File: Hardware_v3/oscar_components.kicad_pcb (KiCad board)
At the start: 4 copper layers, 71 x 100 mm, 71 parts, among them J1 SWD_Header, J10 MIDI_THROUGH, J11 USB_C_Receptacle, J12 Debug_Header, J2 Eurorack_10_pin_power, J3 ChannelC_In, J4 ChannelA_In, J5 ChannelB_In, J6 ChC_Buff_Out, J7 ChA_Buff_Out, J8 ChB_Buff_Out, J9 MIDI_IN, SW1 Reset_Button, SW2 Menu_Button, SW3 Left_Encoder, SW4 Right_Encoder, U1 LT1117-3.3, U2 ILI9341_SPI_Daughterboard, U3 STM32F446RETx, U4 TL074, U5 MCP6004, U6 H11L1, Y1 8MHz

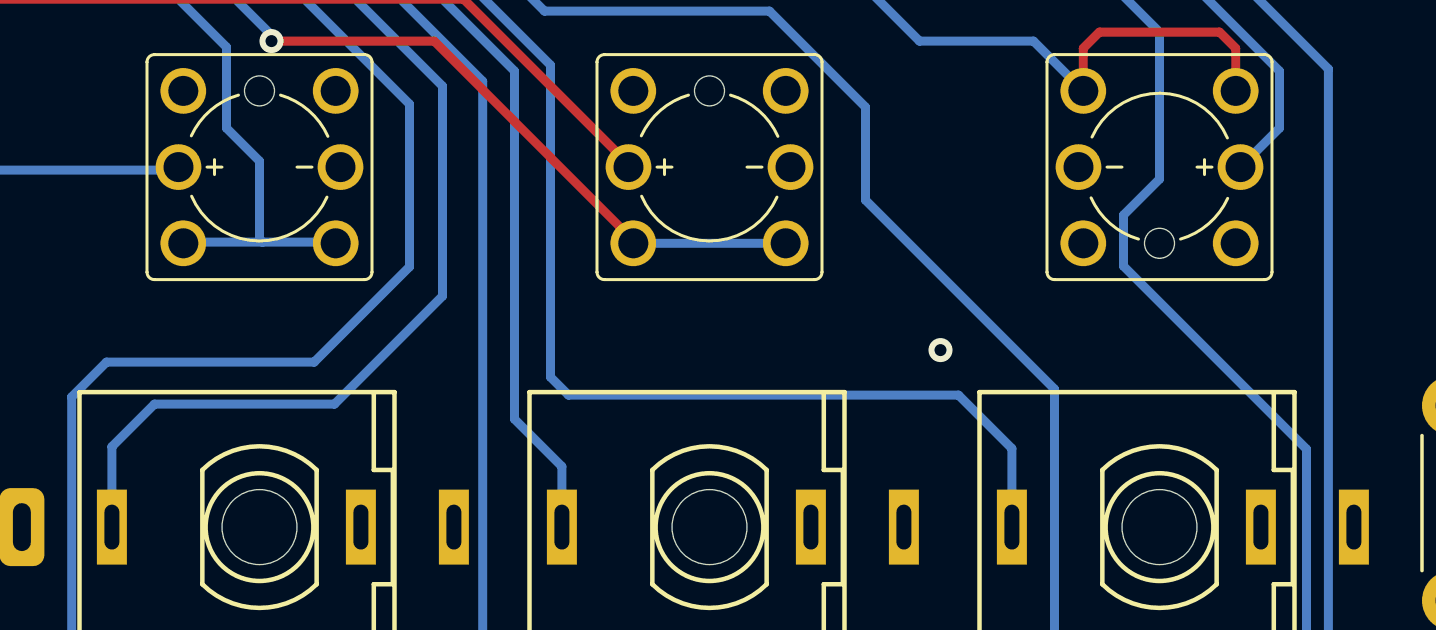
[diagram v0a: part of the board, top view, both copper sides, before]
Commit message: Work on Build Guide; Clean up old folders
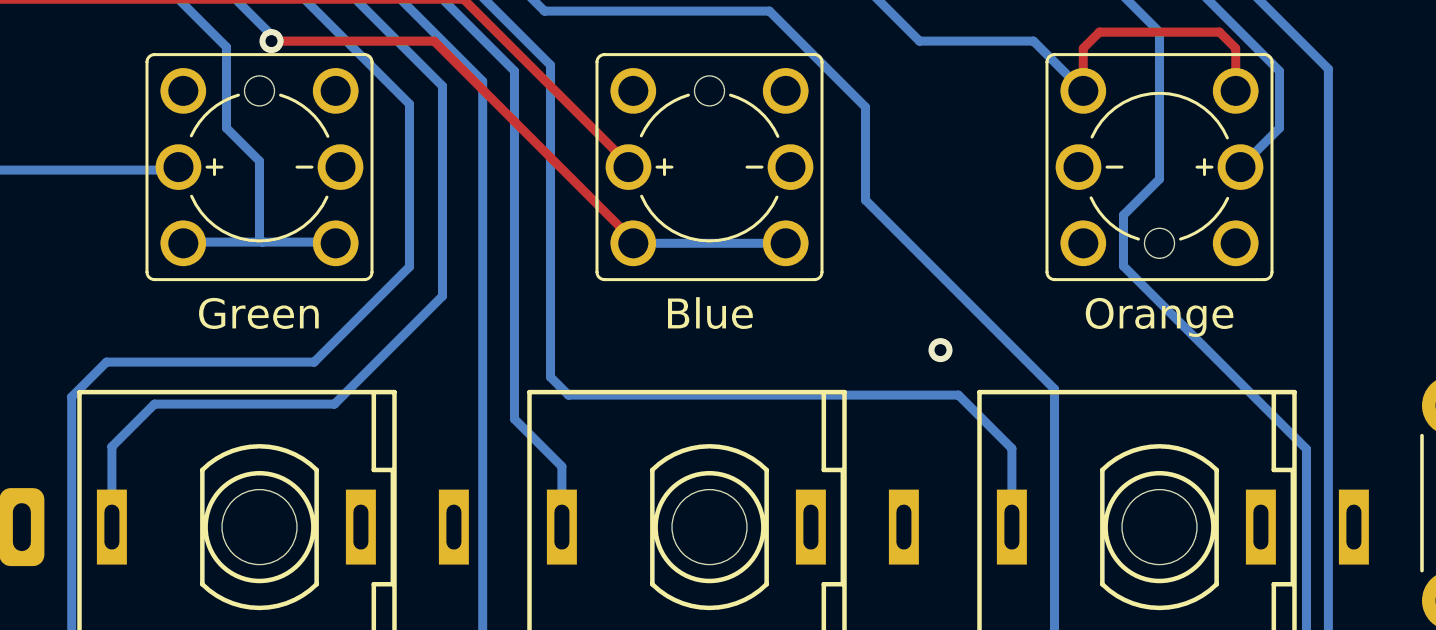
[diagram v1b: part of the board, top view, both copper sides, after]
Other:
- board text added: "Blue"
- board text added: "Green"
- board text added: "Orange"
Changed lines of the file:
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@@
 		(sheetname "Root")
 		(sheetfile "oscar_components.kicad_sch")
-		(attr through_hole)
+		(attr through_hole exclude_from_pos_files exclude_from_bom)
 		(fp_line
 			(start -1.27 1.27)
@@
 		(sheetname "Root")
 		(sheetfile "oscar_components.kicad_sch")
-		(attr through_hole)
+		(attr through_hole exclude_from_pos_files exclude_from_bom)
 		(fp_line
 			(start -5.07 -3.2)
@@
 		(sheetname "Root")
 		(sheetfile "oscar_components.kicad_sch")
-		(attr through_hole)
+		(attr through_hole exclude_from_pos_files exclude_from_bom)
 		(fp_line
 			(start -1.33 -6.41)
@@
 		)
 	)
+	(gr_text "Green"
+		(at 122 125.5 0)
+		(layer "F.SilkS")
+		(effects
+			(font
+				(size 1 1)
+				(thickness 0.15)
+			)
+			(justify bottom)
+		)
+	)
+	(gr_text "Blue"
+		(at 137 125.5 0)
+		(layer "F.SilkS")
+		(effects
+			(font
+				(size 1 1)
+				(thickness 0.15)
+			)
+			(justify bottom)
+		)
+	)
+	(gr_text "Orange"
+		(at 152 125.5 0)
+		(layer "F.SilkS")
+		(effects
+			(font
+				(size 1 1)
+				(thickness 0.15)
+			)
+			(justify bottom)
+		)
+	)

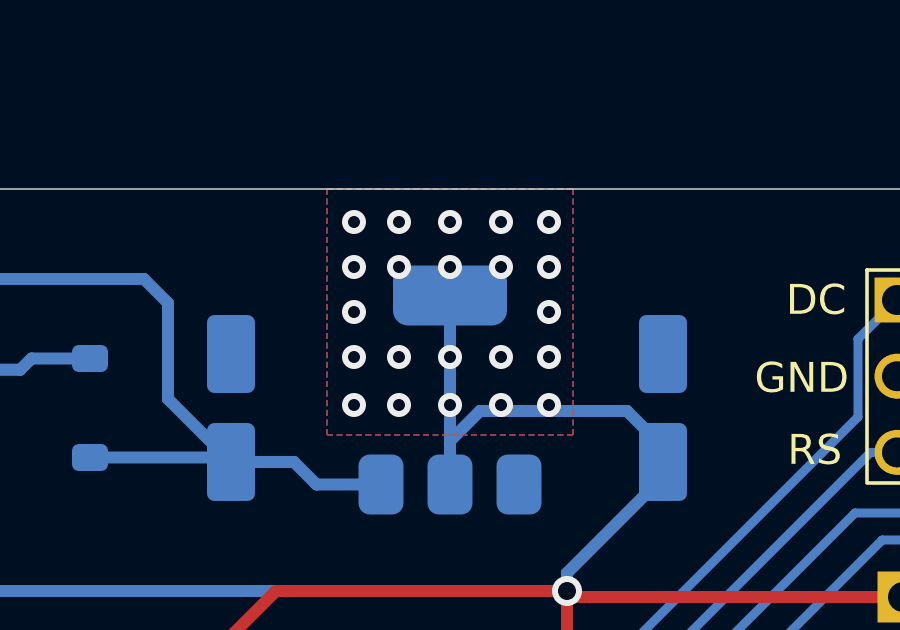
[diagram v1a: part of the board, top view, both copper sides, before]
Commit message: Increased size of regulator heat sink vias
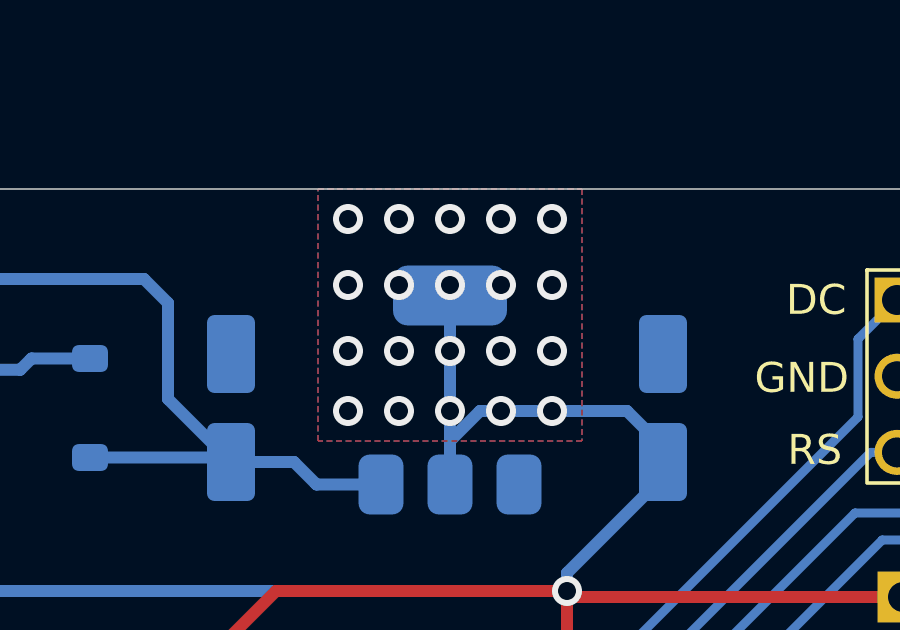
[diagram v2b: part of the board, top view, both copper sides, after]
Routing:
- net +3.3V: vias 28 -> 26
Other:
- board text added: "Oscar v3.1 Mountjoy Modular 2025"
- board text removed: "Oscar v3 Mountjoy Modular 2025"
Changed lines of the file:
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@@
 	)
 	(gr_rect
-		(start 147 50)
-		(end 155.2 58.2)
+		(start 146.8 50)
+		(end 155.4 58.4)
 		(stroke
 			(width 0.2)
@@
 	)
 	(gr_rect
-		(start 147 50)
-		(end 155.2 58.2)
+		(start 146.8 50)
+		(end 155.4 58.4)
 		(stroke
 			(width 0.2)
@@
 		)
 	)
-	(gr_text "Oscar v3\nMountjoy Modular 2025"
+	(gr_text "Oscar v3.1\nMountjoy Modular 2025"
 		(at 124.2 138.1 0)
 		(layer "B.SilkS")
@@
 	)
 	(via
-		(at 154.4 52.6)
-		(size 0.8)
-		(drill 0.4)
+		(at 154.5 53.2)
+		(size 1)
+		(drill 0.6)
 		(layers "F.Cu" "B.Cu")
 		(free yes)
@@
 	)
 	(via
-		(at 149.4 55.6)
-		(size 0.8)
-		(drill 0.4)
+		(at 149.4 55.4)
+		(size 1)
+		(drill 0.6)
 		(layers "F.Cu" "B.Cu")
 		(free yes)
@@
 	)
 	(via
-		(at 147.9 57.2)
-		(size 0.8)
-		(drill 0.4)
+		(at 147.7 57.4)
+		(size 1)
+		(drill 0.6)
 		(layers "F.Cu" "B.Cu")
 		(free yes)
@@
 	)
 	(via
-		(at 154.4 51.1)
-		(size 0.8)
-		(drill 0.4)
+		(at 154.5 51)
+		(size 1)
+		(drill 0.6)
 		(layers "F.Cu" "B.Cu")
 		(free yes)
@@
 	)
 	(via
-		(at 147.9 51.1)
-		(size 0.8)
-		(drill 0.4)
+		(at 147.7 51)
+		(size 1)
+		(drill 0.6)
 		(layers "F.Cu" "B.Cu")
 		(free yes)
@@
 	)
 	(via
-		(at 151.1 55.6)
-		(size 0.8)
-		(drill 0.4)
+		(at 151.1 55.4)
+		(size 1)
+		(drill 0.6)
 		(layers "F.Cu" "B.Cu")
 		(free yes)
@@
 	)
 	(via
-		(at 149.4 51.1)
-		(size 0.8)
-		(drill 0.4)
+		(at 149.4 51)
+		(size 1)
+		(drill 0.6)
 		(layers "F.Cu" "B.Cu")
 		(free yes)
@@
 	)
 	(via
-		(at 151.1 52.6)
-		(size 0.8)
-		(drill 0.4)
+		(at 151.1 53.2)
+		(size 1)
+		(drill 0.6)
 		(layers "F.Cu" "B.Cu")
 		(free yes)
@@
 	)
 	(via
-		(at 154.4 54.1)
-		(size 0.8)
-		(drill 0.4)
-		(layers "F.Cu" "B.Cu")
-		(free yes)
-		(net 10)
-	)
-	(via
-		(at 152.8 57.2)
-		(size 0.8)
-		(drill 0.4)
+		(at 152.8 57.4)
+		(size 1)
+		(drill 0.6)
 		(layers "F.Cu" "B.Cu")
 		(free yes)
@@
 	)
 	(via
-		(at 149.4 57.2)
-		(size 0.8)
-		(drill 0.4)
+		(at 149.4 57.4)
+		(size 1)
+		(drill 0.6)
 		(layers "F.Cu" "B.Cu")
 		(free yes)
@@
 	)
 	(via
-		(at 154.4 57.2)
-		(size 0.8)
-		(drill 0.4)
+		(at 154.5 57.4)
+		(size 1)
+		(drill 0.6)
 		(layers "F.Cu" "B.Cu")
 		(free yes)
@@
 	)
 	(via
-		(at 151.1 57.2)
-		(size 0.8)
-		(drill 0.4)
+		(at 151.1 57.4)
+		(size 1)
+		(drill 0.6)
 		(layers "F.Cu" "B.Cu")
 		(free yes)
@@
 	)
 	(via
-		(at 151.1 51.1)
-		(size 0.8)
-		(drill 0.4)
+		(at 151.1 51)
+		(size 1)
+		(drill 0.6)
 		(layers "F.Cu" "B.Cu")
 		(free yes)
@@
 	)
 	(via
-		(at 149.4 52.6)
-		(size 0.8)
-		(drill 0.4)
-		(layers "F.Cu" "B.Cu")
-		(free yes)
-		(net 10)
-	)
-	(via
-		(at 147.9 52.6)
-		(size 0.8)
-		(drill 0.4)
+		(at 149.4 53.2)
+		(size 1)
+		(drill 0.6)
 		(layers "F.Cu" "B.Cu")
 		(free yes)
@@
 	)
 	(via
-		(at 147.9 54.1)
-		(size 0.8)
-		(drill 0.4)
+		(at 147.7 53.2)
+		(size 1)
+		(drill 0.6)
 		(layers "F.Cu" "B.Cu")
 		(free yes)
@@
 	)
 	(via
-		(at 152.8 55.6)
-		(size 0.8)
-		(drill 0.4)
+		(at 152.8 55.4)
+		(size 1)
+		(drill 0.6)
 		(layers "F.Cu" "B.Cu")
 		(free yes)
@@
 	)
 	(via
-		(at 152.8 52.6)
-		(size 0.8)
-		(drill 0.4)
+		(at 152.8 53.2)
+		(size 1)
+		(drill 0.6)
 		(layers "F.Cu" "B.Cu")
 		(free yes)
@@
 	)
 	(via
-		(at 152.8 51.1)
-		(size 0.8)
-		(drill 0.4)
+		(at 152.8 51)
+		(size 1)
+		(drill 0.6)
 		(layers "F.Cu" "B.Cu")
 		(free yes)
@@
 	)
 	(via
-		(at 154.4 55.6)
-		(size 0.8)
-		(drill 0.4)
+		(at 154.5 55.4)
+		(size 1)
+		(drill 0.6)
 		(layers "F.Cu" "B.Cu")
 		(free yes)
@@
 	)
 	(via
-		(at 147.9 55.6)
-		(size 0.8)
-		(drill 0.4)
+		(at 147.7 55.4)
+		(size 1)
+		(drill 0.6)
 		(layers "F.Cu" "B.Cu")
 		(free yes)
@@
 		(priority 2)
 		(connect_pads yes
-			(clearance 0.5)
+			(clearance 0.2)
 		)
 		(min_thickness 0.25)
@@
 		(polygon
 			(pts
-				(xy 147 50) (xy 155.2 50) (xy 155.2 58.2) (xy 147 58.2)
+				(xy 146.7 50) (xy 155.5 50) (xy 155.5 58.4) (xy 146.7 58.4)
 			)
 		)
